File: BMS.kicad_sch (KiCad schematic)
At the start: 2 parts, among them U2 BQ25895RTW

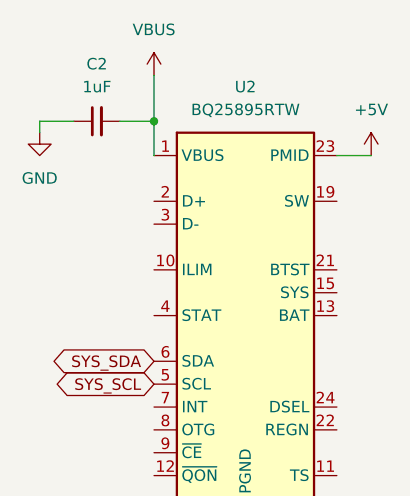
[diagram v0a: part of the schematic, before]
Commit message: flash + bms + usb switch
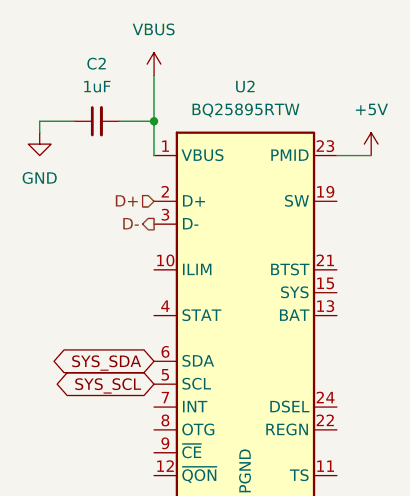
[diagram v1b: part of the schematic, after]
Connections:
- net D+: now reaches U2.2 (D+)
- net D-: now reaches U2.3 (D-)
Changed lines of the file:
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@@
+		)
+	)
+	(hierarchical_label "D-"
+		(shape output)
+		(at 158.75 58.42 180)
+		(fields_autoplaced yes)
+		(effects
+			(font
+				(size 1.27 1.27)
+			)
+			(justify right)
+		)
+	)
+	(hierarchical_label "D+"
+		(shape input)
+		(at 158.75 55.88 180)
+		(fields_autoplaced yes)
+		(effects
+			(font
+				(size 1.27 1.27)
+			)
+			(justify right)
 		)
 	)
@@
 		(dnp no)
 		(fields_autoplaced yes)
-		(property "Reference" "#PWR098"
+		(property "Reference" "#PWR06"
 			(at 146.05 54.61 0)
 			(effects
@@
 			(project ""
 				(path "/e5119d15-74fb-4259-abbc-5cab1f368532/ffb3e92b-c9a0-4fa4-9e23-60cee07ab96a"
-					(reference "#PWR098")
+					(reference "#PWR06")
 					(unit 1)
 				)
@@
 		(dnp no)
 		(fields_autoplaced yes)
-		(property "Reference" "#PWR0105"
+		(property "Reference" "#PWR09"
 			(at 182.88 54.61 0)
 			(effects
@@
 			(project ""
 				(path "/e5119d15-74fb-4259-abbc-5cab1f368532/ffb3e92b-c9a0-4fa4-9e23-60cee07ab96a"
-					(reference "#PWR0105")
+					(reference "#PWR09")
 					(unit 1)
 				)
@@
 		(dnp no)
 		(fields_autoplaced yes)
-		(property "Reference" "#PWR096"
+		(property "Reference" "#PWR08"
 			(at 168.91 97.79 0)
 			(effects
@@
 			(project ""
 				(path "/e5119d15-74fb-4259-abbc-5cab1f368532/ffb3e92b-c9a0-4fa4-9e23-60cee07ab96a"
-					(reference "#PWR096")
+					(reference "#PWR08")
 					(unit 1)
 				)
@@
 		(dnp no)
 		(fields_autoplaced yes)
-		(property "Reference" "#PWR097"
+		(property "Reference" "#PWR07"
 			(at 158.75 45.72 0)
 			(effects
@@
 			(project ""
 				(path "/e5119d15-74fb-4259-abbc-5cab1f368532/ffb3e92b-c9a0-4fa4-9e23-60cee07ab96a"
-					(reference "#PWR097")
-					(unit 1)
-				)
+					(reference "#PWR07")
+					(unit 1)
+				)

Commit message: BMS work
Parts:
- added BATT: 3.7V 5000mAh, symbol Device:Battery_Cell
- added C5: 47nF, symbol Device:C_Small
- added C6, C7, C8: 10uF, symbol Device:C_Small
- added D1: 20v 5A, symbol Device:D_Schottky_Small
- added JP1: Jumper_2_Open, symbol Jumper:Jumper_2_Open
- added L1: 2.2uH, symbol Device:L_Small
- added R3, R4: R_Small, symbol Device:R_Small
- added TH1: 10K NTC, symbol Device:Thermistor_NTC
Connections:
- net +5V: now also D1.1 (K)
- net GND: now also BATT.2 (-), C6.2, C7.2, C8.2, JP1.1 (A), R3.2, TH1.2
- net at U2.11 (TS): now also R3.1, R4.2, TH1.1
- net at U2.12 (~{QON}): now also JP1.2 (B)
- net at U2.13 (BAT), U2.14 (BAT): now also BATT.1 (+), C8.1
- net VBATT: now reaches U2.15 (SYS), U2.16 (SYS)
- net VBATT: now also C6.1, C7.1, L1.2
- net at U2.19 (SW), U2.20 (SW): now also C5.2, D1.2 (A), L1.1
- net at U2.21 (BTST): now also C5.1
- net at U2.22 (REGN): now also R4.1
- net DSEL: now reaches U2.24 (DSEL)
- net INT: now reaches U2.7 (INT)
- net OTG: now reaches U2.8 (OTG)
- net CE: now reaches U2.9 (~{CE})
- net SYS_SCL renamed SCL
- net SYS_SDA renamed SDA
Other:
- moved on the sheet: C2, U2

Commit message: more rp2040 work
-BMS updates
- rp2040 updates
- add hardware design docs
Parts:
- C2: value 1uF -> 1µF
- C6, C7, C8: value 10uF -> 10µF
- JP1: value Jumper_2_Open -> BMS Reset
- L1: value 2.2uH -> 2.2µH
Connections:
- net VBATT renamed +VBATT
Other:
- note added: "+5v from OTG regulator"
- note added: "Thermister in battery TODO: Calculate voltage divider"
- note added: "VBATT 3.5v-4.5v (powers system)"
- note added: "VBUS rails from USB"
- moved on the sheet: BATT, C2, C5, C6, C7, C8, D1, JP1, L1, R3, R4, TH1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

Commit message: BMS updates
- BMS mostly done
- all BMS pins connected to RP2040
- Re-did Minibadge pinouts
- Connected RP2040 to USB Switch
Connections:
- net STAT: now reaches U2.4 (STAT)
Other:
- note added: "TODO: push Batt+/- and TS to JST"
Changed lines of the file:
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@@
+		)
+	)
+	(text "TODO: push Batt+/- and TS to JST"
+		(exclude_from_sim no)
+		(at 226.568 100.33 0)
+		(effects
+			(font
+				(size 1.27 1.27)
+			)
 		)
 	)
@@
 		(shape bidirectional)
 		(at 163.83 92.71 180)
-		(fields_autoplaced yes)
 		(effects
 			(font
@@
 		(shape output)
 		(at 160.02 74.93 180)
-		(fields_autoplaced yes)
+		(effects
+			(font
+				(size 1.27 1.27)
+			)
+			(justify right)
+		)
+	)
+	(hierarchical_label "STAT"
+		(shape output)
+		(at 163.83 85.09 180)
 		(effects
 			(font
@@
 		(shape bidirectional)
 		(at 184.15 95.25 0)
-		(fields_autoplaced yes)
 		(effects
 			(font
@@
 		(shape bidirectional)
 		(at 163.83 95.25 180)
-		(fields_autoplaced yes)
 		(effects
 			(font
@@
 		(shape bidirectional)
 		(at 163.83 90.17 180)
-		(fields_autoplaced yes)
 		(effects
 			(font
@@
 		(shape input)
 		(at 160.02 72.39 180)
-		(fields_autoplaced yes)
 		(effects
 			(font
@@
 	)
 	(hierarchical_label "CE"
-		(shape bidirectional)
+		(shape output)
 		(at 163.83 100.33 180)
-		(fields_autoplaced yes)
 		(effects
 			(font
@@
 		(shape bidirectional)
 		(at 163.83 97.79 180)
-		(fields_autoplaced yes)
 		(effects
 			(font

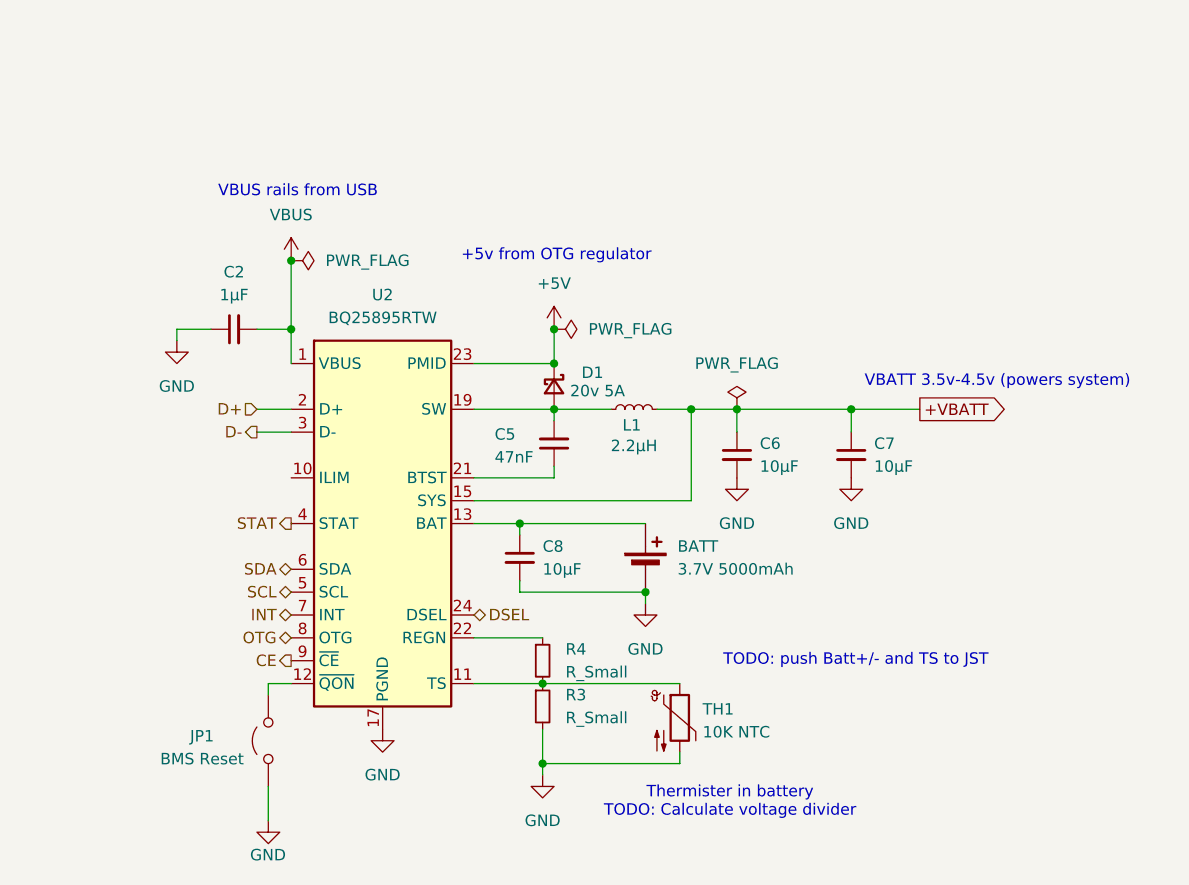
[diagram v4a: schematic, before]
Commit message: BMS updates
Added missing capacitor for OTG
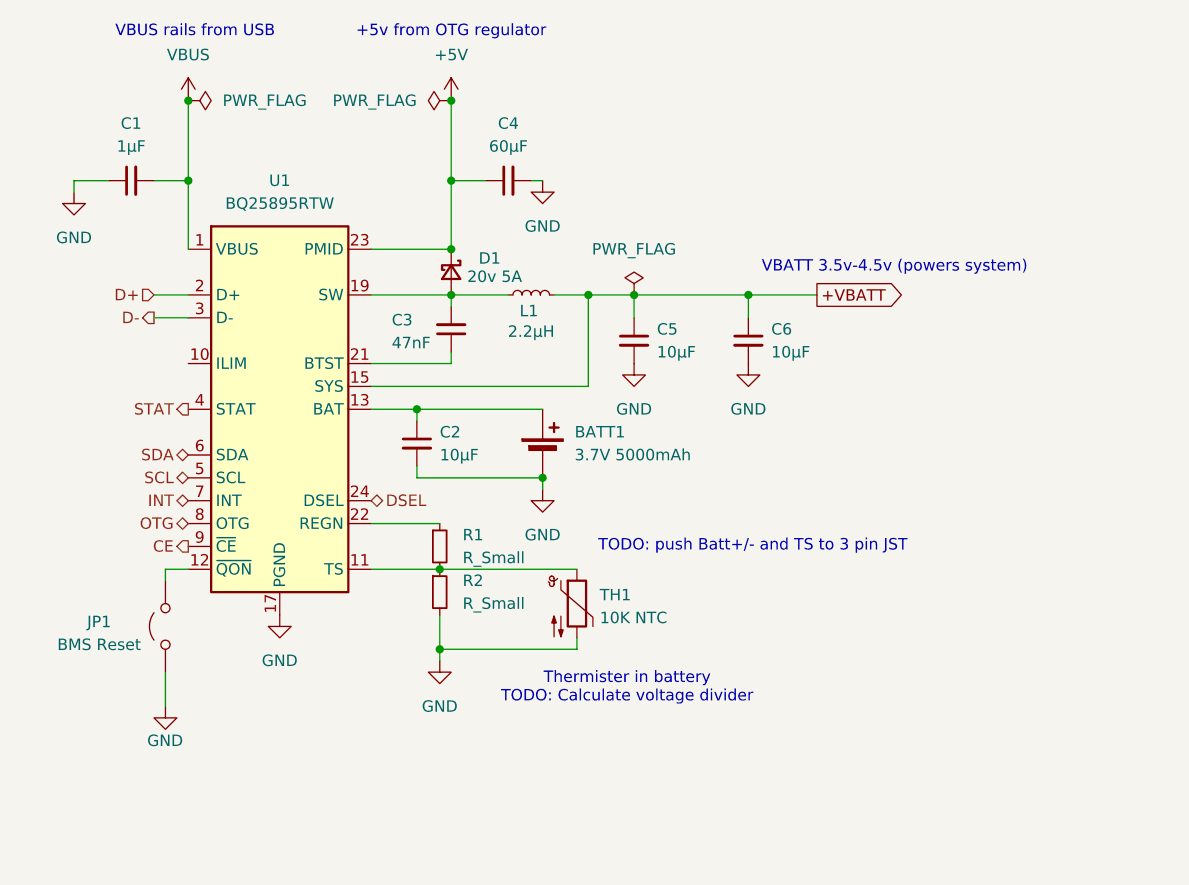
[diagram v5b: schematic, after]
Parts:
- added C4: 60μF, symbol Device:C_Small
- renumbered BATT to BATT1, C2 to C1, C8 to C2, C5 to C3, C6 to C5, C7 to C6, R4 to R1, R3 to R2, U2 to U1
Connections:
- net +5V: now also C4.1
- net GND: now also C4.2
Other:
- note added: "TODO: push Batt+/- and TS to 3 pin JST"
- note removed: "TODO: push Batt+/- and TS to JST"
- moved on the sheet: BATT1, C1, C2, C3, C5, C6, D1, JP1, L1, R1, R2, TH1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
